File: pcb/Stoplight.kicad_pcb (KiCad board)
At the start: 2 copper layers, 15 x 15 mm, 18 parts, among them IC1 ATtiny85-20M, IC2 AP7375-33SA-7

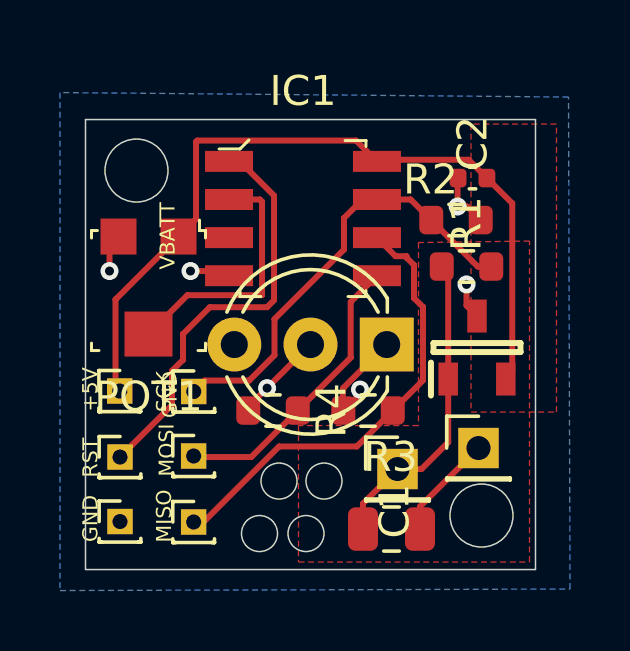
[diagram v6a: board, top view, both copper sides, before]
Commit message: Ordered v1, updated part numbers to reflect availability
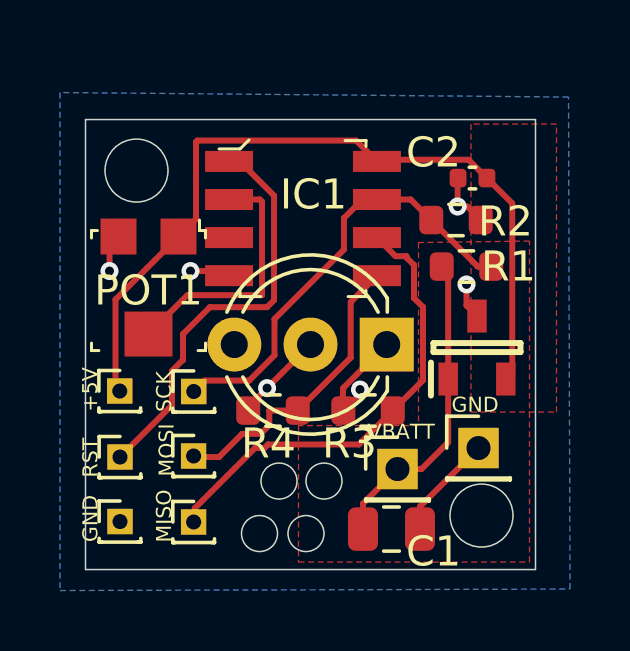
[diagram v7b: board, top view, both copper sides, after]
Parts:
- C1: value 2.2uF,100V -> 2.2uF, 50V
- R3: value 65 -> 150
- R4: value 65 -> 85
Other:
- board text added: "Stoplight v1 Max Batchelder"
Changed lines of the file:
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@@
 		(descr "http://ww1.microchip.com/downloads/en/DeviceDoc/Atmel-2586-AVR-8-bit-Microcontroller-ATtiny25-ATtiny45-ATtiny85_Datasheet-Summary.pdf")
 		(property "Reference" "IC1"
-			(at 0 -4.25 0)
+			(at 0.35 -0.8 0)
 			(layer "F.SilkS")
 			(effects
@@
 		(descr "http://www.bourns.com/docs/Product-Datasheets/TC33.pdf")
 		(property "Reference" "POT1"
-			(at 0 -3.54 180)
+			(at 0 0 180)
 			(layer "F.SilkS")
 			(effects
@@
 		(tags "resistor")
 		(property "Reference" "R3"
-			(at 0.75 1.55 0)
+			(at -0.618279 1.1 0)
 			(layer "F.SilkS")
 			(effects
@@
 			)
 		)
-		(property "Value" "65"
+		(property "Value" "150"
 			(at 0 1.43 0)
 			(layer "F.Fab")
@@
 			)
 		)
-		(property "Part Number" "ERJ-1GNF64R9C"
+		(property "Part Number" "ERA-3AEB151V"
 			(at 0 0 0)
 			(unlocked yes)
@@
 			)
 		)
-		(property "URL" "https://www.digikey.com/en/products/detail/panasonic-electronic-components/ERJ-1GNF64R9C/2035977"
+		(property "URL" "https://www.digikey.com/en/products/detail/panasonic-electronic-components/ERA-3AEB151V/1465834"
 			(at 0 0 0)
 			(unlocked yes)
@@
 		(tags "resistor")
 		(property "Reference" "R2"
-			(at -0.85 -1.35 360)
+			(at 1.65 0.05 0)
 			(layer "F.SilkS")
 			(effects
@@
 		)
 		(property "Value" "3K3 0.1%"
-			(at 0 1.43 360)
+			(at 0 1.43 0)
 			(layer "F.Fab")
 			(effects
@@
 		)
 		(fp_text user "${REFERENCE}"
-			(at 0 0 360)
+			(at 0 0 0)
 			(layer "F.Fab")
 			(effects
@@
 		(tags "resistor")
 		(property "Reference" "R4"
-			(at 1.95 0 90)
+			(at -0.15 1.1 180)
 			(layer "F.SilkS")
 			(effects
@@
 			)
 		)
-		(property "Value" "65"
+		(property "Value" "85"
 			(at 0 1.43 0)
 			(layer "F.Fab")
@@
 			)
 		)
-		(property "Part Number" "ERJ-1GNF64R9C"
+		(property "Part Number" "ERJ-3EKF84R5V"
 			(at 0 0 0)
 			(unlocked yes)
@@
 			)
 		)
-		(property "URL" "https://www.digikey.com/en/products/detail/panasonic-electronic-components/ERJ-1GNF64R9C/2035977"
+		(property "URL" "https://www.digikey.com/en/products/detail/panasonic-electronic-components/ERJ-3EKF84R5V/196495"
 			(at 0 0 0)
 			(unlocked yes)
@@
 		(tags "Integrated Circuit")
 		(property "Reference" "IC2"
-			(at 0 0 270)
+			(at 0 0 -90)
 			(layer "F.SilkS")
 			(hide yes)
@@
 		)
 		(property "Value" "AP7375-33SA-7"
-			(at 0 0 270)
+			(at 0 0 -90)
 			(layer "F.SilkS")
 			(hide yes)
@@
 		)
 		(property "Footprint" "AP7375-33SA-7:SOT96P240X110-3N"
-			(at 0 0 270)
+			(at 0 0 -90)
 			(layer "F.Fab")
 			(hide yes)
@@
 		)
 		(property "Datasheet" "https://www.diodes.com/assets/Datasheets/AP7375.pdf"
-			(at 0 0 270)
+			(at 0 0 -90)
 			(layer "F.Fab")
 			(hide yes)
@@
 		)
 		(property "Description" "LDO Voltage Regulators LDO CMOS LowCurr SOT23 T&R 3K"
-			(at 0 0 270)
+			(at 0 0 -90)
 			(layer "F.Fab")
 			(hide yes)
@@
 		)
 		(fp_text user "${REFERENCE}"
-			(at 0 0 270)
+			(at 0 0 -90)
 			(layer "F.Fab")
 			(effects
@@
 		(tags "resistor")
 		(property "Reference" "R1"
-			(at 0 -1.43 90)
+			(at 1.4 0 180)
 			(layer "F.SilkS")
 			(effects
@@
 		)
 		(property "Value" "10K .1%"
-			(at 0 1.43 360)
+			(at 0 1.43 0)
 			(layer "F.Fab")
 			(effects
@@
 		)
 		(fp_text user "${REFERENCE}"
-			(at 0 0 360)
+			(at 0 0 0)
 			(layer "F.Fab")
 			(effects
@@
 		(tags "capacitor")
 		(property "Reference" "C1"
-			(at -0.1 0.6 -90)
+			(at -1.4 -0.75 0)
 			(layer "F.SilkS")
 			(effects
@@
 			)
 		)
-		(property "Value" "2.2uF,100V"
+		(property "Value" "2.2uF, 50V"
 			(at 0 1.68 180)
 			(layer "F.Fab")
@@
 			)
 		)
-		(property "URL" "https://www.digikey.com/en/products/detail/tdk-corporation/C2012X7R2A225K125AC/20482638"
+		(property "URL" "https://www.digikey.com/en/products/detail/taiyo-yuden/UMK212BB7225KG-T/3194965"
 			(at 0 0 180)
 			(unlocked yes)
@@
 		(tags "capacitor")
 		(property "Reference" "C2"
-			(at 0 -1.16 90)
+			(at -1.3 -0.85 180)
 			(layer "F.SilkS")
 			(effects
@@
 		)
 		(property "Value" "22uF,10V+"
-			(at 0 1.16 360)
+			(at 0 1.16 0)
 			(layer "F.Fab")
 			(effects
@@
 			)
 		)
-		(property "Part Number" "GRM158R61A226ME15D"
+		(property "Part Number" "GMC04X5R226M10NT"
 			(at 0 0 0)
 			(unlocked yes)
@@
 			)
 		)
-		(property "URL" "https://www.digikey.com/en/products/detail/murata-electronics/GRM158R61A226ME15D/16033379"
+		(property "URL" "https://www.digikey.com/en/products/detail/cal-chip-electronics-inc/GMC04X5R226M10NT/23571654"
 			(at 0 0 0)
 			(unlocked yes)
@@
 		)
 		(fp_text user "${REFERENCE}"
-			(at 0 0 360)
+			(at 0 0 0)
 			(layer "F.Fab")
 			(effects
@@
 		(layer "Edge.Cuts")
 	)
+	(gr_text "Stoplight v1\nMax Batchelder"
+		(at 139.4 83.1 0)
+		(layer "B.SilkS")
+		(effects
+			(font
+				(size 1 1)
+				(thickness 0.15)
+			)
+			(justify left bottom mirror)
+		)
+	)
 	(gr_text "+5V"
 		(at 126.95 89.335 -90)
@@
 	)
 	(gr_text "GND"
-		(at 127.5135 89.55 -90)
+		(at 139 89.5 0)
 		(layer "B.SilkS")
 		(effects
@@
 	)
 	(gr_text "VBATT"
-		(at 127.586 84.6 -90)
+		(at 136.8 90.3 0)
 		(layer "B.SilkS")
 		(effects
@@
 	)
 	(gr_text "VBATT"
-		(at 128.2275 84.6 90)
+		(at 134.6 90.3 0)
 		(layer "F.SilkS")
 		(effects
@@
 	)
 	(gr_text "GND"
-		(at 128.3 89.55 90)
+		(at 137.4 89.4 0)
 		(layer "F.SilkS")
 		(effects
@@
 	)
 	(segment
+		(start 129.65 90.85)
+		(end 130.425 90.075)
+		(width 0.2)
+		(layer "F.Cu")
+		(net 7)
+	)
+	(segment
+		(start 131.325 89.3)
+		(end 132.275 89.3)
+		(width 0.2)
+		(layer "F.Cu")
+		(net 7)
+	)
+	(segment
 		(start 134.915 84.805)
 		(end 134.04 85.68)
@@
 	)
 	(segment
-		(start 128.84 90.85)
-		(end 130.725 90.85)
+		(start 131.037648 90.075)
+		(end 131.325 89.787648)
 		(width 0.2)
 		(layer "F.Cu")
@@
 	)
 	(segment
-		(start 130.725 90.85)
-		(end 132.275 89.3)
+		(start 128.84 90.85)
+		(end 129.65 90.85)
 		(width 0.2)
 		(layer "F.Cu")
@@
 	)
 	(segment
+		(start 131.325 89.787648)
+		(end 131.325 89.3)
+		(width 0.2)
+		(layer "F.Cu")
+		(net 7)
+	)
+	(segment
+		(start 130.425 90.075)
+		(end 131.037648 90.075)
+		(width 0.2)
+		(layer "F.Cu")
+		(net 7)
+	)
+	(segment
 		(start 134.04 87.535)
 		(end 132.275 89.3)
@@
 	)
 	(segment
+		(start 134.312543 90.430736)
+		(end 135.443279 89.3)
+		(width 0.2)
+		(layer "F.Cu")
+		(net 9)
+	)
+	(segment
+		(start 130.850939 90.549061)
+		(end 131.165279 90.549061)
+		(width 0.2)
+		(layer "F.Cu")
+		(net 9)
+	)
+	(segment
 		(start 136.15 84.45)
 		(end 136.15 85.55)
@@
 	)
 	(segment
-		(start 135.535 84.155)
-		(end 135.9 84.155)
+		(start 128.84 93.05)
+		(end 128.84 92.56)
 		(width 0.2)
 		(layer "F.Cu")
@@
 	)
 	(segment
-		(start 129.1 93.05)
-		(end 131.652433 90.497567)
+		(start 135.535 84.155)
+		(end 135.9 84.155)
 		(width 0.2)
 		(layer "F.Cu")
@@
 	)
 	(segment
-		(start 134.245712 90.497567)
-		(end 135.443279 89.3)
+		(start 128.84 92.56)
+		(end 130.850939 90.549061)
 		(width 0.2)
 		(layer "F.Cu")
@@
 	)
 	(segment
-		(start 131.652433 90.497567)
-		(end 134.245712 90.497567)
+		(start 136.15 85.55)
+		(end 136.45 85.85)
 		(width 0.2)
 		(layer "F.Cu")
@@
 	)
 	(segment
-		(start 136.15 85.55)
-		(end 136.45 85.85)
+		(start 128.805 93.015)
+		(end 128.84 93.05)
 		(width 0.2)
 		(layer "F.Cu")
@@
 	)
 	(segment
-		(start 128.805 93.015)
-		(end 128.84 93.05)
+		(start 131.283604 90.430736)
+		(end 134.312543 90.430736)
 		(width 0.2)
 		(layer "F.Cu")
@@
 	)
 	(segment
-		(start 128.84 93.05)
-		(end 129.1 93.05)
+		(start 131.165279 90.549061)
+		(end 131.283604 90.430736)
 		(width 0.2)
 		(layer "F.Cu")

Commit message: pcb v1a
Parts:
- removed TP3: GND, Connector_PinHeader_1.00mm:PinHeader_1x01_P1.00mm_Vertical
- removed TP4: 3V3, Connector_PinHeader_1.00mm:PinHeader_1x01_P1.00mm_Vertical
- removed TP5: MISO, Connector_PinHeader_1.00mm:PinHeader_1x01_P1.00mm_Vertical
- removed TP6: MOSI, Connector_PinHeader_1.00mm:PinHeader_1x01_P1.00mm_Vertical
- removed TP7: SCK, Connector_PinHeader_1.00mm:PinHeader_1x01_P1.00mm_Vertical
- removed TP8: RST, Connector_PinHeader_1.00mm:PinHeader_1x01_P1.00mm_Vertical
- added REF**: PinHeader_1x06_P2.54mm_Vertical, Connector_PinHeader_2.54mm:PinHeader_1x06_P2.54mm_Vertical, F.Cu at (127.4, 99.6)
- C1: footprint Capacitor_SMD:C_0805_2012Metric -> Capacitor_THT:C_Radial_D5.0mm_H5.0mm_P2.00mm
- C2: footprint Capacitor_SMD:C_0402_1005Metric -> Capacitor_THT:C_Radial_D5.0mm_H5.0mm_P2.00mm
- IC1: footprint digikey-footprints:SOIC-8_W5.3mm -> digikey-footprints:DIP-8_W7.62mm
- IC2: footprint AP7375-33SA-7:SOT96P240X110-3N -> Package_TO_SOT_SMD:TSOT-23_HandSoldering
- R1, R2, R3, R4: footprint Resistor_SMD:R_0603_1608Metric -> Resistor_THT:R_Axial_DIN0204_L3.6mm_D1.6mm_P5.08mm_Horizontal
- moved R4 31.8 mm to (160.9, 101.2), turned to 180 degrees
- moved R3 27.7 mm to (160.9, 97.8), turned to 180 degrees
- moved R1 23.9 mm to (143.5, 107.7)
- moved R2 21.3 mm to (155.9, 93.8)
- moved D1 20.2 mm to (155.4, 87.1)
- moved C1 17.1 mm to (138.3, 110.1), turned to 0 degrees
- moved IC1 17.0 mm to (144.8, 94.6)
- moved IC2 17.0 mm to (138.8, 104.2), turned to -90 degrees
- moved C2 16.8 mm to (134.2, 97.9)
- moved POT1 16.2 mm to (143.4, 87.4)
- moved TP1 8.96 mm to (141.0, 98.4)
- moved TP2 1.33 mm to (139.4, 91.3)
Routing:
- net SCK/BATT: track 14.8 -> 40.4 mm
- net MOSI/R: track 10.0 -> 33.9 mm
- net +5V: track 26.9 -> 49.3 mm
- net MISO/G: track 15.5 -> 37.9 mm
- net Net-(D1-A2): track 3.06 -> 17.4 mm, vias 1 -> 0
- net RST: track 13.9 -> 26.9 mm
- net Net-(D1-A1): track 3.77 -> 13.0 mm, vias 1 -> 0
- net +VBATT: track 10.5 -> 19.2 mm
- net GND: track 9.24 -> 2.80 mm, vias 4 -> 2
- net DIM: track 8.57 -> 9.70 mm
- removed copper zone on F.Cu, net +5V
- removed copper zone on F.Cu, net +VBATT
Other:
- board size 15 x 15 mm -> 39.7 x 33.1 mm
- board text added: "5V"
- board text added: "Stoplight v1a Max Batchelder"
- board text removed: "+5V"
- board text removed: "Stoplight v1 Max Batchelder"
